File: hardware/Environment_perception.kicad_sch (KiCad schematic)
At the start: 0 parts

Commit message: Added IMU and barometer, and connected to STM32
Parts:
- added C37, C38, C39: 100nF, symbol Device:C
- added U3: LSM6DSO32TR, LGA-14L_2P5X3X0P83_STM, symbol 2026-10-14_19-08-18:LSM6DSO32TR
- added U4: (no value), symbol Sensor:MS5837-02BA21
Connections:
- new net +3V3: C37.1, C38.1, C39.1, U3.5 (VDDIO), U3.8 (VDD), U4.2 (VDD)
- new net BAROMETER_SCL: U4.3 (SCL)
- new net BAROMETER_SDA: U4.4 (SDA)
- new net GND: C37.2, C38.2, C39.2, U3.2 (SDx), U3.3 (SCx), U3.6 (GND), U3.7 (GND), U4.1 (GND)
- new net IMU_CS1: U3.12 (CS)
- new net IMU_INT1: U3.4 (INT1)
- new net IMU_INT2: U3.9 (INT2)
- new net IMU_MISO: U3.1 (SDO/SA0)
- new net IMU_MOSI: U3.14 (SDA)
- new net IMU_NC10: U3.10 (NC)
- new net IMU_NC11: U3.11 (NC)
- new net IMU_SCK: U3.13 (SCL)
- no-connect marks 0 -> 2
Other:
- note added: "Barometer"
- note added: "IMU"
- note added: "Operating in "mode 1" with 4-wire SPI"

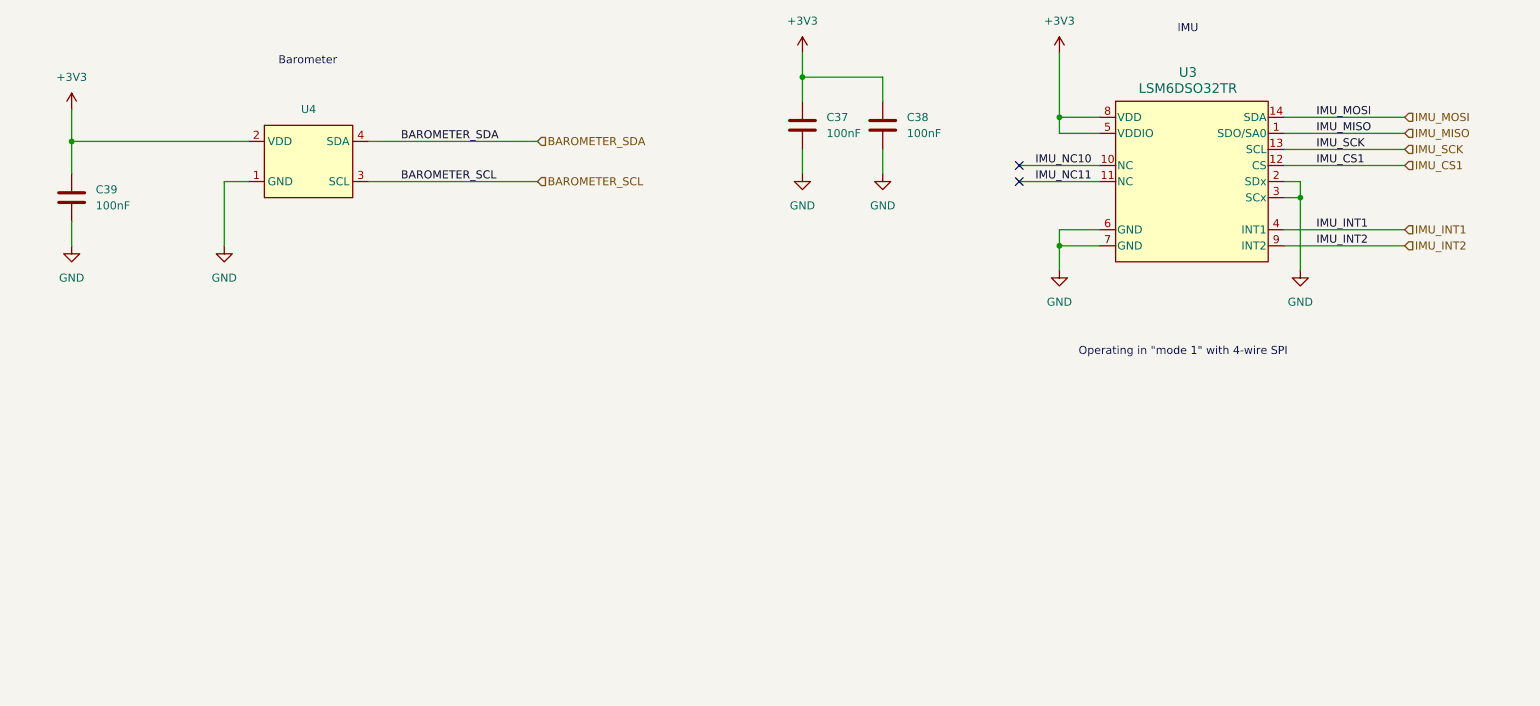
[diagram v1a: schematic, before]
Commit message: Updated IMU to BMI270 for supply chain reason
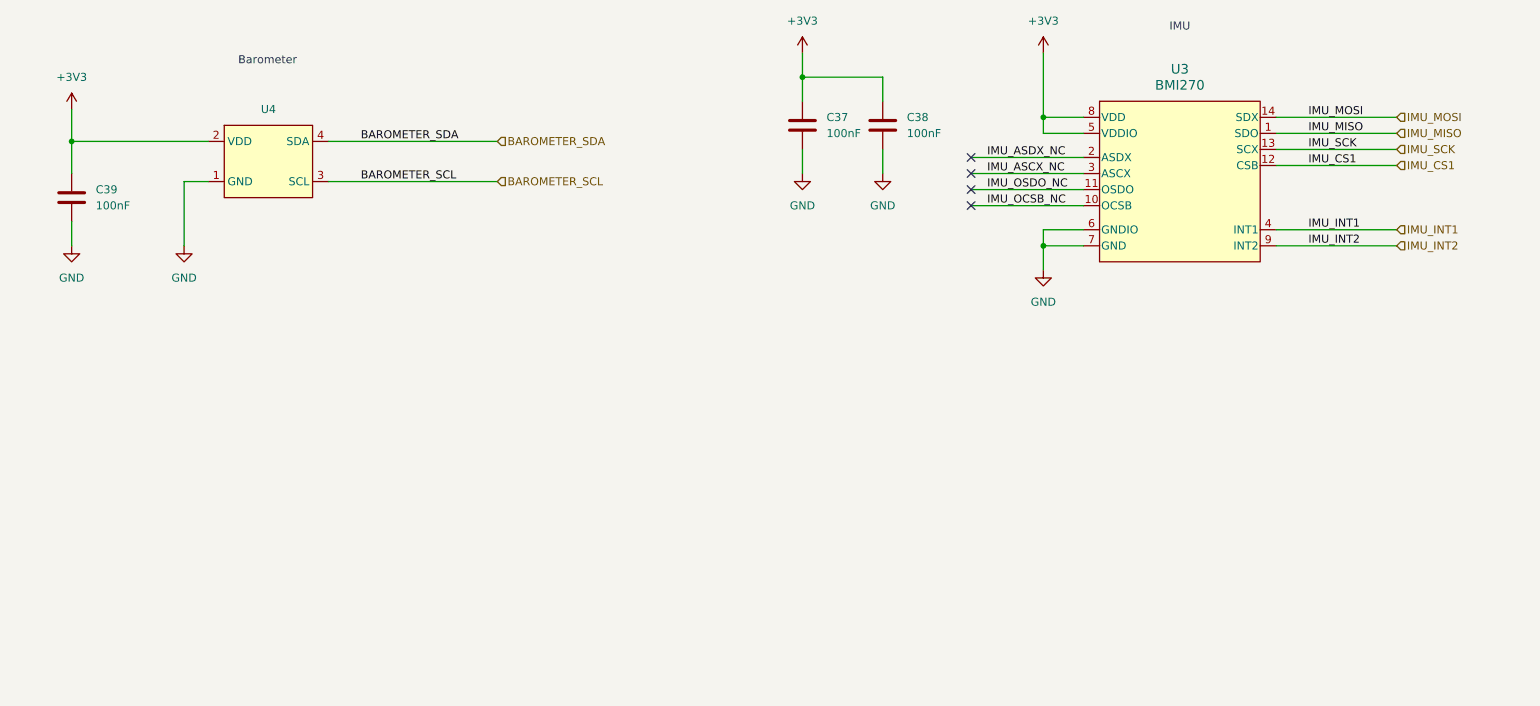
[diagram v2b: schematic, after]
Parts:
- removed U3: LSM6DSO32TR, LGA-14L_2P5X3X0P83_STM, symbol 2026-10-14_19-08-18:LSM6DSO32TR
- added U3: BMI270, BMI270_BOS, symbol BMI270:BMI270
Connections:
- net +3V3: now also U3.5 (VDDIO), U3.8 (VDD)
- net GND: now also U3.6 (GNDIO), U3.7 (GND)
- net IMU_CS1: now also U3.12 (CSB)
- net IMU_INT1: now also U3.4 (INT1)
- net IMU_INT2: now also U3.9 (INT2)
- net IMU_MISO: now also U3.1 (SDO)
- net IMU_MOSI: now also U3.14 (SDX)
- net IMU_SCK: now also U3.13 (SCX)
- new net IMU_ASCX_NC: U3.3 (ASCX)
- new net IMU_ASDX_NC: U3.2 (ASDX)
- new net IMU_OCSB_NC: U3.10 (OCSB)
- new net IMU_OSDO_NC: U3.11 (OSDO)
- no-connect marks 2 -> 4
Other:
- note removed: "Operating in "mode 1" with 4-wire SPI"
- moved on the sheet: U4

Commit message: Changing barometer, STM32 and power rails
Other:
- note added: "TODO: Both Barometer and BMI270 are compatible with 1p8"
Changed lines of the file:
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@@
+		)
+	)
+	(text "TODO:\nBoth Barometer and BMI270 are compatible with 1p8"
+		(exclude_from_sim no)
+		(at 178.054 170.18 0)
+		(effects
+			(font
+				(size 1.27 1.27)
+			)
+			(justify left)
 		)
 	)

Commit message: Added optical front end submodule and reconnected to STM32
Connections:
- net +3V3 renamed +1V8

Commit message: Added bosch barometer
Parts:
- removed U4: (no value), symbol Sensor:MS5837-02BA21
- added C46: 100nF, symbol Device:C
- added R13, R14: 0, symbol Device:R_US
- added U4: BMP585, BMP585:XDCR_BMP585, symbol BMP585:BMP585
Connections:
- net +1V8: now also C46.1, R13.1, U4.4 (VDDIO), U4.7 (CSB), U4.8 (VDD)
- net BAROMETER_SCL: now also U4.1 (SCX)
- net BAROMETER_SDA: now also U4.2 (SDX)
- net GND: now also C46.2, R14.2, U4.6 (VSSIO/VSS)
- new net BAROMETER_INT: U4.5 (INT)
- new net BAROMETER_L/M: U4.9 (L/M)
- new net BAROMETER_SDO: R13.2, R14.1, U4.3 (SDO)
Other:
- note added: "I2C address set to 0x46 when SDO is 0V 0x47 when SDO is tied to VDD"
- moved on the sheet: C37, C38, C39, U3

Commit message: Contemplating switching back to the 64LQFP
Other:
- note removed: "TODO: Both Barometer and BMI270 are compatible with 1p8"
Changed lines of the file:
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@@
-		)
-	)
-	(text "TODO:\nBoth Barometer and BMI270 are compatible with 1p8"
-		(exclude_from_sim no)
-		(at 178.054 170.18 0)
-		(effects
-			(font
-				(size 1.27 1.27)
-			)
-			(justify left)
 		)
 	)

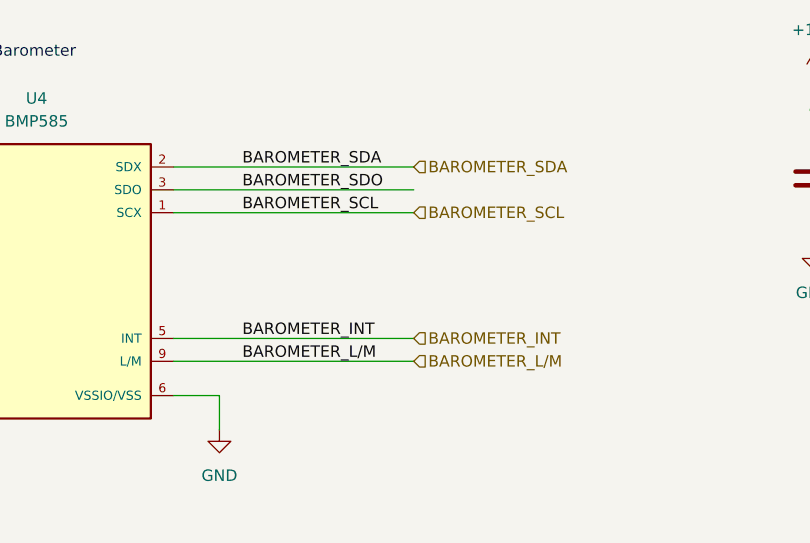
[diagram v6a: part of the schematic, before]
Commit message: Added level translator, connected all misc GPIO. Ensured that 64QLFP has support for 1.8V
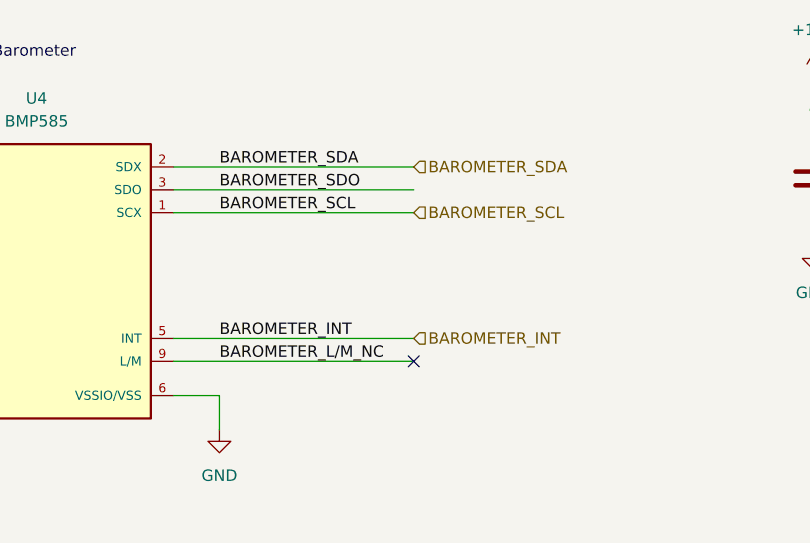
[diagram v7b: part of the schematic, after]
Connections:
- net BAROMETER_L/M renamed BAROMETER_L/M_NC
- no-connect marks 4 -> 5
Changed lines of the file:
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@@
+	)
+	(no_connect
+		(at 119.38 102.87)
 	)
 	(no_connect
@@
 	)
 	(label "BAROMETER_SDO"
-		(at 100.33 83.82 0)
+		(at 97.79 83.82 0)
 		(effects
 			(font
@@
 	)
 	(label "BAROMETER_INT"
-		(at 100.33 100.33 0)
+		(at 97.79 100.33 0)
 		(effects
 			(font
@@
 		)
 	)
-	(label "BAROMETER_L{slash}M"
-		(at 100.33 102.87 0)
+	(label "BAROMETER_L{slash}M_NC"
+		(at 97.79 102.87 0)
 		(effects
 			(font
@@
 	)
 	(label "BAROMETER_SDA"
-		(at 100.33 81.28 0)
+		(at 97.79 81.28 0)
 		(effects
 			(font
@@
 	)
 	(label "BAROMETER_SCL"
-		(at 100.33 86.36 0)
+		(at 97.79 86.36 0)
 		(effects
 			(font
@@
 		(effects
 			(font
-				(size 1.27 1.27)
-			)
-			(justify left)
-		)
-	)
-	(hierarchical_label "BAROMETER_L{slash}M"
-		(shape input)
-		(at 119.38 102.87 0)
-		(effects
-			(font
